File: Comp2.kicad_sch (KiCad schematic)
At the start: 1 part, among them U3 ADUM3190ARQZ-RL7

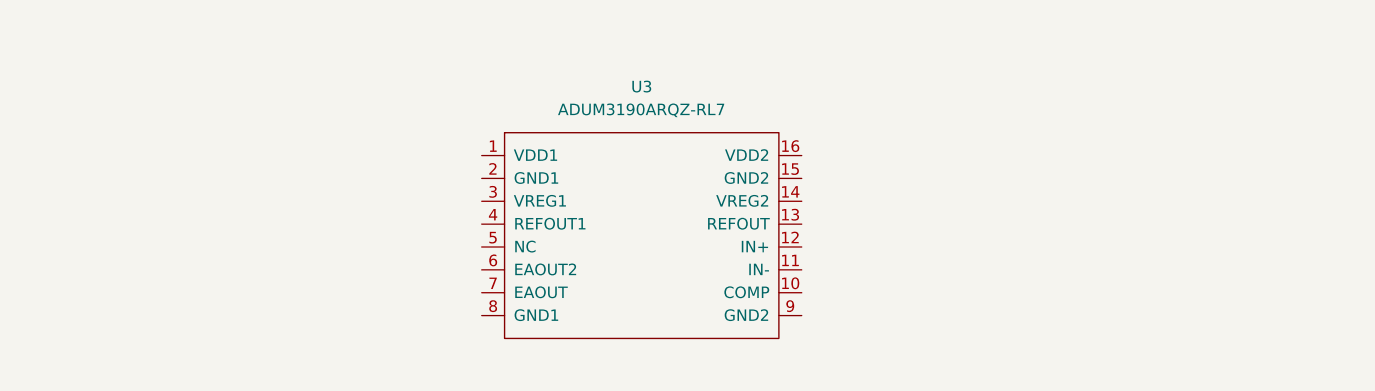
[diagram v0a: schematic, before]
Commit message: 完善补偿电路原理图；
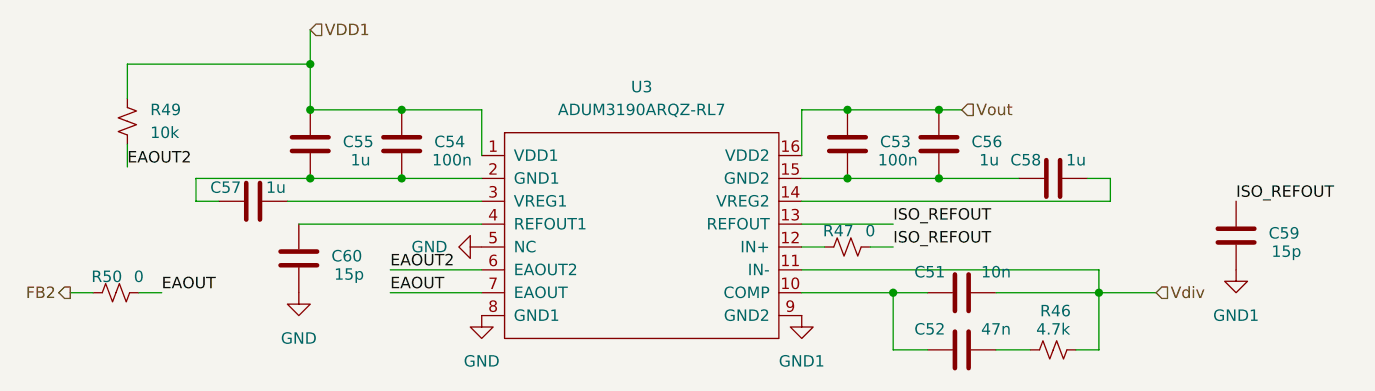
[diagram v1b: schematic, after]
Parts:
- added C51: 10n, Capacitor_SMD:C_0603_1608Metric_Pad1.08x0.95mm_HandSolder, symbol Device:C
- added C52: 47n, Capacitor_SMD:C_0603_1608Metric_Pad1.08x0.95mm_HandSolder, symbol Device:C
- added C53, C54: 100n, Capacitor_SMD:C_0603_1608Metric_Pad1.08x0.95mm_HandSolder, symbol Device:C
- added C55, C56, C57, C58: 1u, Capacitor_SMD:C_0603_1608Metric_Pad1.08x0.95mm_HandSolder, symbol Device:C
- added C59, C60: 15p, Capacitor_SMD:C_0603_1608Metric_Pad1.08x0.95mm_HandSolder, symbol Device:C
- added R46: 4.7k, Resistor_SMD:R_0603_1608Metric_Pad0.98x0.95mm_HandSolder, symbol Device:R_Small_US
- added R47, R50: 0, Resistor_SMD:R_0603_1608Metric_Pad0.98x0.95mm_HandSolder, symbol Device:R_Small_US
- added R49: 10k, Resistor_SMD:R_0603_1608Metric_Pad0.98x0.95mm_HandSolder, symbol Device:R_Small_US
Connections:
- net VDD1: now reaches U3.1 (VDD1)
- net VDD1: now also C54.2, C55.2, R49.2
- net at U3.10 (COMP): now also C51.2, C52.2
- net Vdiv: now reaches U3.11 (IN-)
- net Vdiv: now also C51.1, R46.1
- net at U3.12 (IN+): now also R47.2
- net ISO_REFOUT: now reaches U3.13 (REFOUT)
- net ISO_REFOUT: now also C59.2, R47.1
- net at U3.14 (VREG2): now also C58.1
- net at U3.15 (GND2): now also C53.1, C56.1, C58.2
- net Vout: now reaches U3.16 (VDD2)
- net Vout: now also C53.2, C56.2
- net at U3.2 (GND1): now also C54.1, C55.1, C57.2
- net at U3.3 (VREG1): now also C57.1
- net at U3.4 (REFOUT1): now also C60.2
- net GND: now reaches U3.5 (NC)
- net GND: now also U3.8 (GND1), C60.1
- net EAOUT2: now reaches U3.6 (EAOUT2)
- net EAOUT2: now also R49.1
- net EAOUT: now reaches U3.7 (EAOUT)
- net EAOUT: now also R50.1
- net GND1: now reaches U3.9 (GND2)
- net GND1: now also C59.1
- new net: C52.1, R46.2
- new net FB2: R50.2

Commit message: 初版布局连线；
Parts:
- R47: footprint Resistor_SMD:R_0603_1608Metric_Pad0.98x0.95mm_HandSolder -> Resistor_SMD:R_0402_1005Metric_Pad0.72x0.64mm_HandSolder
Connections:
- net GND: now also C54.1, C55.1, C57.2, U3.2 (GND1)
- net GND1: now also C53.1, C56.1, C58.2, U3.15 (GND2)
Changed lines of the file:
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@@
 	(paper "A4")
+	(junction
+		(at 187.96 68.58)
+		(diameter 0)
+		(color 0 0 0 0)
+	)
 	(junction
 		(at 181.61 60.96)
@@
 	(wire
 		(pts
-			(xy 190.5 68.58) (xy 181.61 68.58)
-		)
-		(stroke
-			(width 0)
-			(type default)
-		)
-	)
-	(wire
-		(pts
 			(xy 171.45 68.58) (xy 181.61 68.58)
 		)
@@
 		(pts
 			(xy 198.12 68.58) (xy 200.66 68.58)
+		)
+		(stroke
+			(width 0)
+			(type default)
+		)
+	)
+	(wire
+		(pts
+			(xy 181.61 68.58) (xy 190.5 68.58)
 		)
 		(stroke
@@
 	)
 	(symbol
+		(lib_id "power:GND")
+		(at 121.92 68.58 0)
+		(unit 1)
+		(body_style 1)
+		(exclude_from_sim no)
+		(in_bom yes)
+		(on_board yes)
+		(in_pos_files yes)
+		(dnp no)
+		(fields_autoplaced yes)
+		(property "Reference" "#PWR038"
+			(at 121.92 74.93 0)
+			(hide yes)
+			(show_name no)
+			(do_not_autoplace no)
+			(effects
+				(font
+					(size 1.27 1.27)
+				)
+			)
+		)
+		(property "Value" "GND"
+			(at 121.92 73.66 0)
+			(show_name no)
+			(do_not_autoplace no)
+			(effects
+				(font
+					(size 1.27 1.27)
+				)
+			)
+		)
+		(property "Footprint" ""
+			(at 121.92 68.58 0)
+			(hide yes)
+			(show_name no)
+			(do_not_autoplace no)
+			(effects
+				(font
+					(size 1.27 1.27)
+				)
+			)
+		)
+		(property "Datasheet" ""
+			(at 121.92 68.58 0)
+			(hide yes)
+			(show_name no)
+			(do_not_autoplace no)
+			(effects
+				(font
+					(size 1.27 1.27)
+				)
+			)
+		)
+		(property "Description" "Power symbol creates a global label with name \"GND\" , ground"
+			(at 121.92 68.58 0)
+			(hide yes)
+			(show_name no)
+			(do_not_autoplace no)
+			(effects
+				(font
+					(size 1.27 1.27)
+				)
+			)
+		)
+		(pin "1"
+		)
+		(instances
+			(project "FlyBack_pic16f1769"
+				(path "/85fd1e61-7f7c-4adf-9ad3-eb5962af39d5/b3af68bd-246f-4e85-8862-676fb544c4e8"
+					(reference "#PWR038")
+					(unit 1)
+				)
+			)
+		)
+	)
+	(symbol
 		(lib_id "Device:R_Small_US")
 		(at 194.31 87.63 270)
@@
 	)
 	(symbol
+		(lib_id "power:GND1")
+		(at 187.96 68.58 180)
+		(unit 1)
+		(body_style 1)
+		(exclude_from_sim no)
+		(in_bom yes)
+		(on_board yes)
+		(in_pos_files yes)
+		(dnp no)
+		(fields_autoplaced yes)
+		(property "Reference" "#PWR037"
+			(at 187.96 62.23 0)
+			(hide yes)
+			(show_name no)
+			(do_not_autoplace no)
+			(effects
+				(font
+					(size 1.27 1.27)
+				)
+			)
+		)
+		(property "Value" "GND1"
+			(at 187.96 63.5 0)
+			(show_name no)
+			(do_not_autoplace no)
+			(effects
+				(font
+					(size 1.27 1.27)
+				)
+			)
+		)
+		(property "Footprint" ""
+			(at 187.96 68.58 0)
+			(hide yes)
+			(show_name no)
+			(do_not_autoplace no)
+			(effects
+				(font
+					(size 1.27 1.27)
+				)
+			)
+		)
+		(property "Datasheet" ""
+			(at 187.96 68.58 0)
+			(hide yes)
+			(show_name no)
+			(do_not_autoplace no)
+			(effects
+				(font
+					(size 1.27 1.27)
+				)
+			)
+		)
+		(property "Description" "Power symbol creates a global label with name \"GND1\" , ground"
+			(at 187.96 68.58 0)
+			(hide yes)
+			(show_name no)
+			(do_not_autoplace no)
+			(effects
+				(font
+					(size 1.27 1.27)
+				)
+			)
+		)
+		(pin "1"
+		)
+		(instances
+			(project "FlyBack_pic16f1769"
+				(path "/85fd1e61-7f7c-4adf-9ad3-eb5962af39d5/b3af68bd-246f-4e85-8862-676fb544c4e8"
+					(reference "#PWR037")
+					(unit 1)
+				)
+			)
+		)
+	)
+	(symbol
 		(lib_id "power:GND")
 		(at 130.81 83.82 0)
@@
 			)
 		)
-		(property "Footprint" "Resistor_SMD:R_0603_1608Metric_Pad0.98x0.95mm_HandSolder"
+		(property "Footprint" "Resistor_SMD:R_0402_1005Metric_Pad0.72x0.64mm_HandSolder"
 			(at 171.45 76.2 0)
 			(hide yes)
